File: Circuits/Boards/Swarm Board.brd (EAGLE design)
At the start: 76.2 x 76.2 mm, 95 parts, among them CON1 ISP(2X3), T1 NPN2N2222, T10 TEFT4300, T11 NPN2N2222, T12 NPN2N2222, T13 NPN2N2222, T14 NPN2N2222, T15 NPN2N2222, T16 NPN2N2222, T17 NPN2N2222, T18 NPN2N2222, T2 NPN2N2222, T3 NPN2N2222, T4 TEFT4300, T5 TEFT4300, T6 TEFT4300, T7 TEFT4300, T8 TEFT4300, T9 TEFT4300, U1 ATMEGA324P, U2 MCP73832SOT-23, U3 TB6552FN/FNG

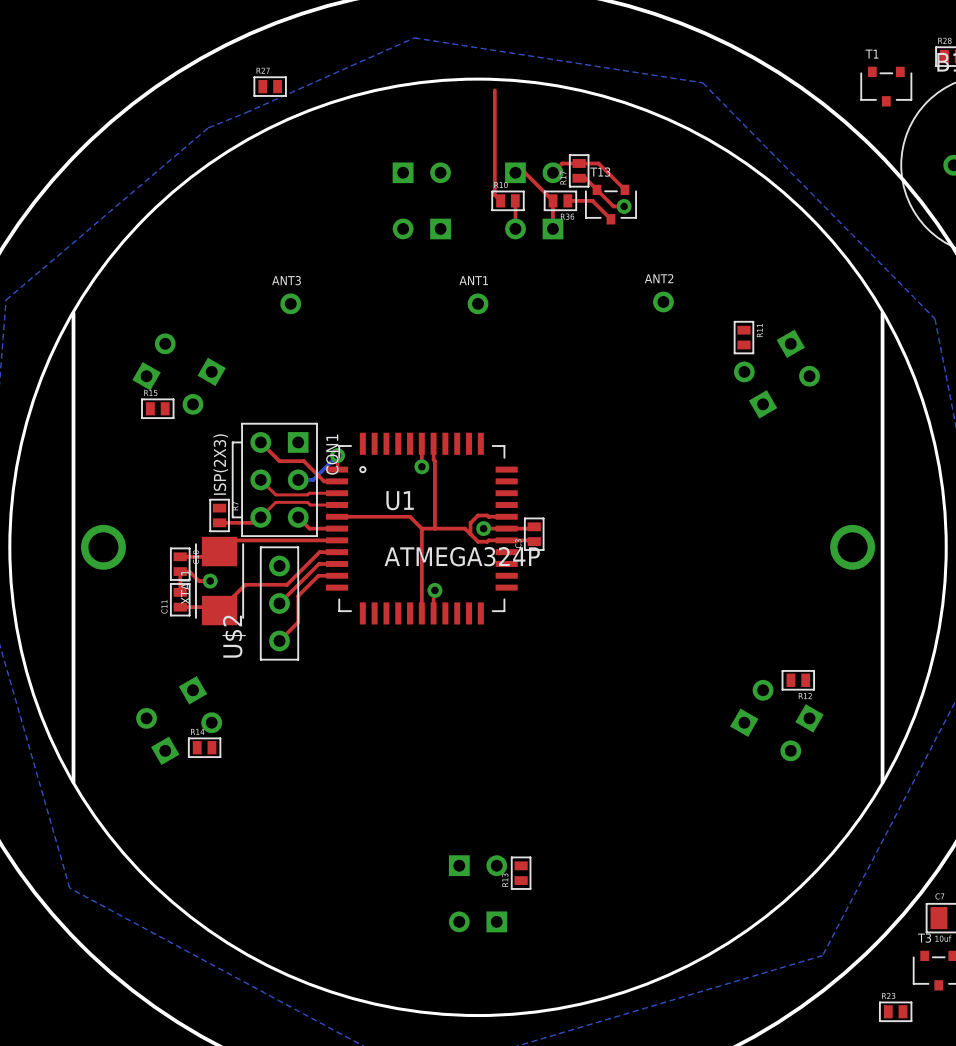
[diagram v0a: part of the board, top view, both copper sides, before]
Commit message: 
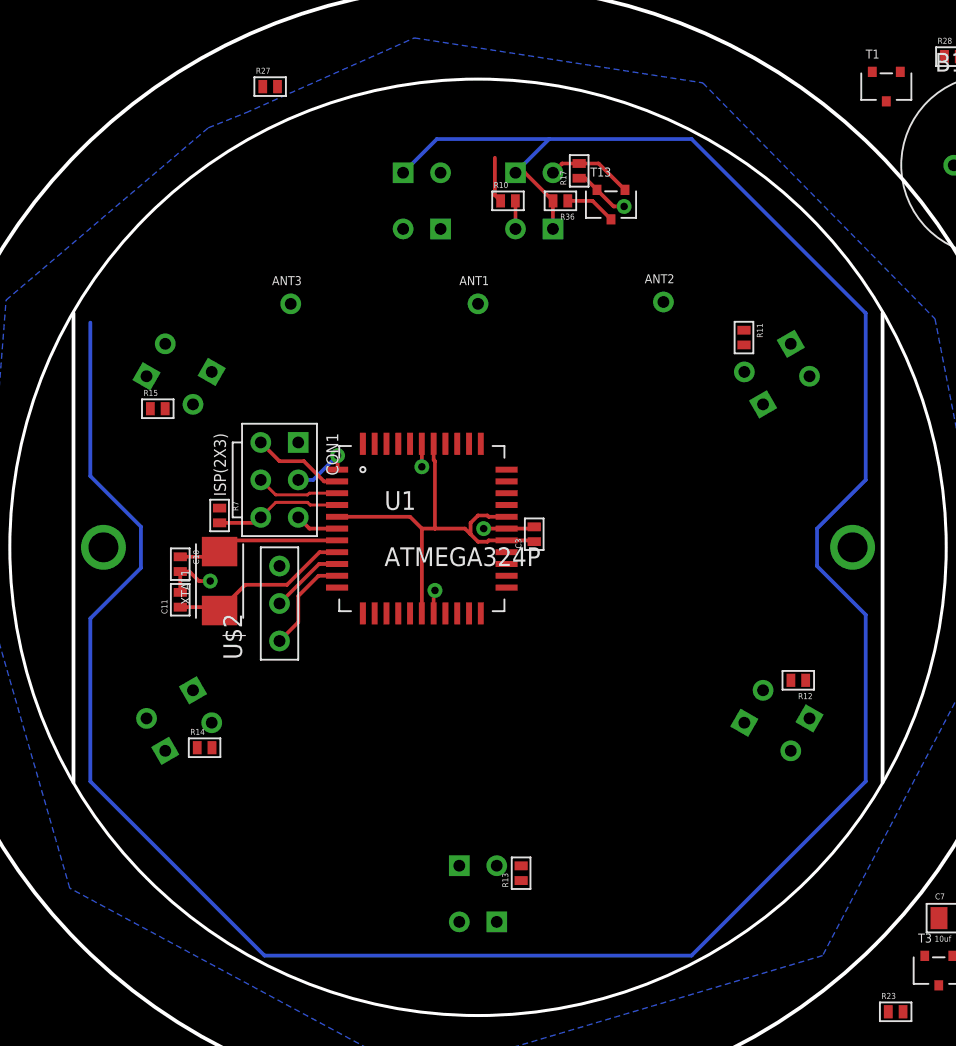
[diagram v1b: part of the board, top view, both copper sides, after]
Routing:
- net +3V: track 34.4 -> 205.6 mm
- net N$10: track 7.66 -> 3.09 mm
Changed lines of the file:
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@@
 <wire x1="36.838" y1="55.245" x2="34.933" y2="57.15" width="0.254" layer="1"/>
 <wire x1="34.933" y1="57.15" x2="34.29" y2="57.15" width="0.254" layer="1"/>
+<wire x1="36.576" y1="59.436" x2="46.228" y2="59.436" width="0.254" layer="16"/>
+<wire x1="46.228" y1="59.436" x2="58.039" y2="47.625" width="0.254" layer="16"/>
+<wire x1="36.576" y1="59.436" x2="34.29" y2="57.15" width="0.254" layer="16"/>
+<wire x1="26.67" y1="57.15" x2="28.956" y2="59.436" width="0.254" layer="16"/>
+<wire x1="28.956" y1="59.436" x2="36.576" y2="59.436" width="0.254" layer="16"/>
+<wire x1="58.039" y1="47.625" x2="58.039" y2="36.322" width="0.254" layer="16"/>
+<wire x1="58.039" y1="36.322" x2="54.737" y2="33.02" width="0.254" layer="16"/>
+<wire x1="54.737" y1="33.02" x2="54.737" y2="30.48" width="0.254" layer="16"/>
+<wire x1="54.737" y1="30.48" x2="58.039" y2="27.178" width="0.254" layer="16"/>
+<wire x1="58.039" y1="27.178" x2="58.039" y2="15.875" width="0.254" layer="16"/>
+<wire x1="58.039" y1="15.875" x2="46.228" y2="4.064" width="0.254" layer="16"/>
+<wire x1="46.228" y1="4.064" x2="17.272" y2="4.064" width="0.254" layer="16"/>
+<wire x1="17.272" y1="4.064" x2="5.461" y2="15.875" width="0.254" layer="16"/>
+<wire x1="5.461" y1="15.875" x2="5.461" y2="26.924" width="0.254" layer="16"/>
+<wire x1="5.461" y1="26.924" x2="8.89" y2="30.353" width="0.254" layer="16"/>
+<wire x1="8.89" y1="30.353" x2="8.89" y2="33.147" width="0.254" layer="16"/>
+<wire x1="8.89" y1="33.147" x2="5.461" y2="36.576" width="0.254" layer="16"/>
+<wire x1="5.461" y1="36.576" x2="5.461" y2="46.99" width="0.254" layer="16"/>
 <wire x1="92.472" y1="42.418" x2="94.168" y2="44.189" width="0" layer="19" extent="1-1"/>
 <wire x1="80.637" y1="46.736" x2="92.472" y2="42.418" width="0" layer="19" extent="1-1"/>
@@
 <wire x1="69.969" y1="64.516" x2="80.7212" y2="56.769" width="0" layer="19" extent="1-1"/>
 <wire x1="64.008" y1="57.658" x2="69.969" y2="64.516" width="0" layer="19" extent="1-1"/>
+<wire x1="58.039" y1="47.625" x2="64.008" y2="57.658" width="0" layer="19" extent="16-16"/>
+<wire x1="29.21" y1="53.34" x2="26.67" y2="57.15" width="0" layer="19" extent="1-1"/>
+<wire x1="9.271" y1="43.350146875" x2="5.461" y2="46.99" width="0" layer="19" extent="16-16"/>
+<wire x1="13.6906" y1="43.64485" x2="9.271" y2="43.350146875" width="0" layer="19" extent="1-1"/>
+<wire x1="52.959" y1="45.54985" x2="58.039" y2="47.625" width="0" layer="19" extent="16-16"/>
+<wire x1="51.0794" y1="41.445146875" x2="52.959" y2="45.54985" width="0" layer="19" extent="1-1"/>
+<wire x1="14.224" y1="34.409" x2="8.89" y2="33.147" width="0" layer="19" extent="1-16"/>
+<wire x1="10.541" y1="17.950146875" x2="5.461" y2="15.875" width="0" layer="19" extent="16-16"/>
+<wire x1="12.4206" y1="22.05485" x2="10.541" y2="17.950146875" width="0" layer="19" extent="1-1"/>
+<wire x1="54.229" y1="20.14985" x2="58.039" y2="15.875" width="0" layer="19" extent="16-16"/>
+<wire x1="49.8094" y1="19.855146875" x2="54.229" y2="20.14985" width="0" layer="19" extent="1-1"/>
+<wire x1="22.19" y1="33.82" x2="14.224" y2="34.409" width="0" layer="19" extent="1-1"/>
+<wire x1="63.008" y1="6.604" x2="58.039" y2="15.875" width="0" layer="19" extent="1-16"/>
+<wire x1="74.565" y1="8.89" x2="63.008" y2="6.604" width="0" layer="19" extent="1-1"/>
+<wire x1="33.02" y1="6.35" x2="46.228" y2="4.064" width="0" layer="19" extent="16-16"/>
+<wire x1="30.48" y1="10.16" x2="33.02" y2="6.35" width="0" layer="19" extent="1-1"/>
 <wire x1="87.003" y1="28.321" x2="92.472" y2="42.418" width="0" layer="19" extent="1-1"/>
 <wire x1="94.226" y1="26.416" x2="87.003" y2="28.321" width="0" layer="19" extent="1-1"/>
@@
 <wire x1="76.846" y1="24.871" x2="77.605" y2="28.321" width="0" layer="19" extent="1-1"/>
 <wire x1="73.795" y1="24.384" x2="76.846" y2="24.871" width="0" layer="19" extent="1-1"/>
-<wire x1="74.565" y1="8.89" x2="73.795" y2="24.384" width="0" layer="19" extent="1-1"/>
-<wire x1="63.008" y1="6.604" x2="74.565" y2="8.89" width="0" layer="19" extent="1-1"/>
-<wire x1="54.229" y1="20.14985" x2="63.008" y2="6.604" width="0" layer="19" extent="1-1"/>
-<wire x1="49.8094" y1="19.855146875" x2="54.229" y2="20.14985" width="0" layer="19" extent="1-1"/>
-<wire x1="52.959" y1="45.54985" x2="64.008" y2="57.658" width="0" layer="19" extent="1-1"/>
-<wire x1="51.0794" y1="41.445146875" x2="52.959" y2="45.54985" width="0" layer="19" extent="1-1"/>
-<wire x1="36.83" y1="53.34" x2="52.959" y2="45.54985" width="0" layer="19" extent="1-1"/>
-<wire x1="29.21" y1="53.34" x2="34.29" y2="57.15" width="0" layer="19" extent="1-1"/>
-<wire x1="26.67" y1="57.15" x2="29.21" y2="53.34" width="0" layer="19" extent="1-1"/>
-<wire x1="28.74" y1="38.77" x2="29.21" y2="53.34" width="0" layer="19" extent="1-1"/>
-<wire x1="14.224" y1="34.409" x2="22.19" y2="33.82" width="0" layer="19" extent="1-1"/>
-<wire x1="13.6906" y1="43.64485" x2="14.224" y2="34.409" width="0" layer="19" extent="1-1"/>
-<wire x1="9.271" y1="43.350146875" x2="13.6906" y2="43.64485" width="0" layer="19" extent="1-1"/>
-<wire x1="12.4206" y1="22.05485" x2="14.224" y2="34.409" width="0" layer="19" extent="1-1"/>
-<wire x1="10.541" y1="17.950146875" x2="12.4206" y2="22.05485" width="0" layer="19" extent="1-1"/>
-<wire x1="30.48" y1="10.16" x2="27.94" y2="27.27" width="0" layer="19" extent="1-1"/>
-<wire x1="33.02" y1="6.35" x2="30.48" y2="10.16" width="0" layer="19" extent="1-1"/>
 <wire x1="95.361" y1="7.89" x2="97.401" y2="26.289" width="0" layer="19" extent="1-1"/>
-<wire x1="-86.114" y1="-10.922" x2="10.541" y2="17.950146875" width="0" layer="19" extent="1-1"/>
+<wire x1="-86.114" y1="-10.922" x2="5.461" y2="15.875" width="0" layer="19" extent="1-16"/>
 <wire x1="-88.908" y1="-10.922" x2="-86.114" y2="-10.922" width="0" layer="19" extent="1-1"/>
 <wire x1="-91.702" y1="-10.922" x2="-88.908" y2="-10.922" width="0" layer="19" extent="1-1"/>
@@
 <contactref element="R15" pad="1"/>
 <contactref element="T2" pad="3"/>
+<wire x1="33.282" y1="55.245" x2="33.274" y2="55.245" width="0.254" layer="1"/>
+<wire x1="33.274" y1="55.245" x2="32.893" y2="55.626" width="0.254" layer="1"/>
+<wire x1="32.893" y1="55.626" x2="32.893" y2="58.166" width="0.254" layer="1"/>
+<wire x1="33.282" y1="55.245" x2="49.784" y2="46.474" width="0" layer="19" extent="1-1"/>
 <wire x1="53.967" y1="22.733" x2="49.784" y2="46.474" width="0" layer="19" extent="1-1"/>
 <wire x1="34.671" y1="9.152" x2="53.967" y2="22.733" width="0" layer="19" extent="1-1"/>
@@
 <wire x1="9.533" y1="41.148" x2="12.708" y2="18.161" width="0" layer="19" extent="1-1"/>
 <wire x1="81.153" y1="3.318" x2="53.967" y2="22.733" width="0" layer="19" extent="1-1"/>
-<wire x1="33.282" y1="55.245" x2="33.274" y2="55.245" width="0.254" layer="1"/>
-<wire x1="33.274" y1="55.245" x2="32.893" y2="55.626" width="0.254" layer="1"/>
-<wire x1="32.893" y1="55.626" x2="32.893" y2="62.738" width="0.254" layer="1"/>
-<wire x1="32.893" y1="62.738" x2="49.784" y2="46.474" width="0" layer="19" extent="1-16"/>
 </signal>
 <signal name="N$11">

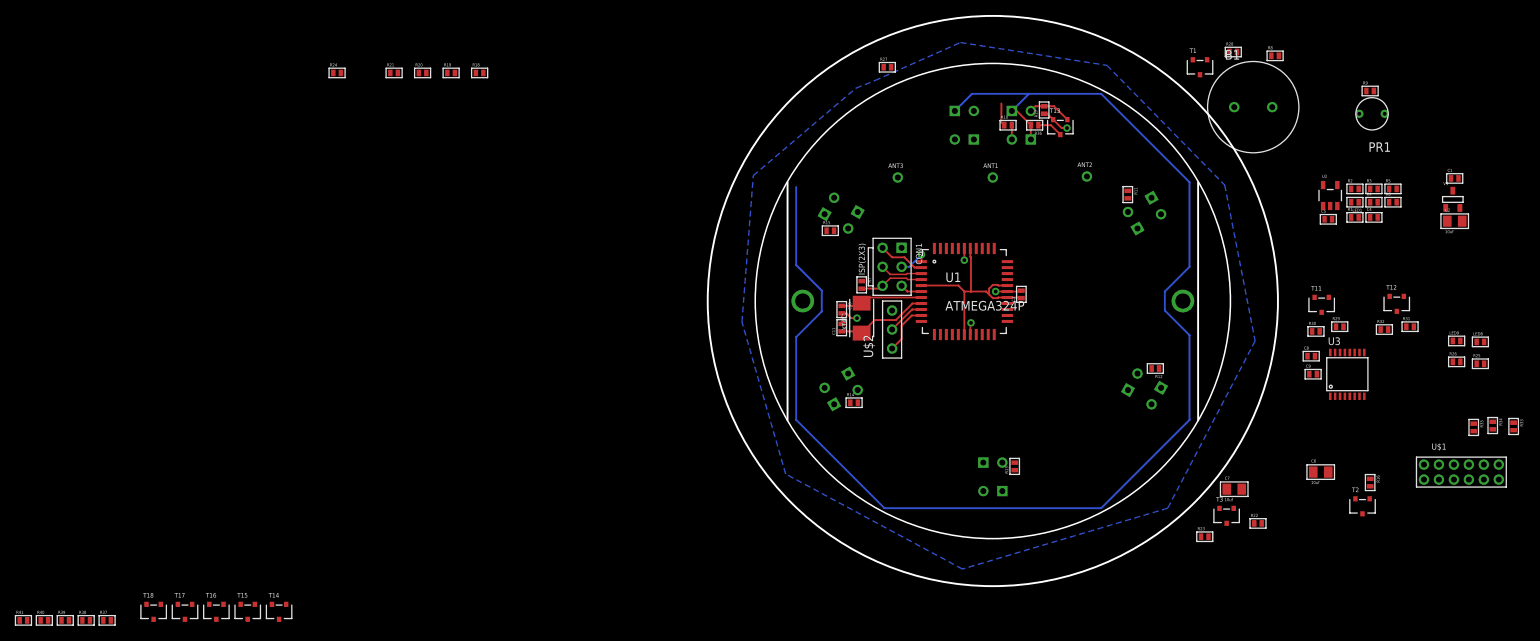
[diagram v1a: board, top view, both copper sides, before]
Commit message: 
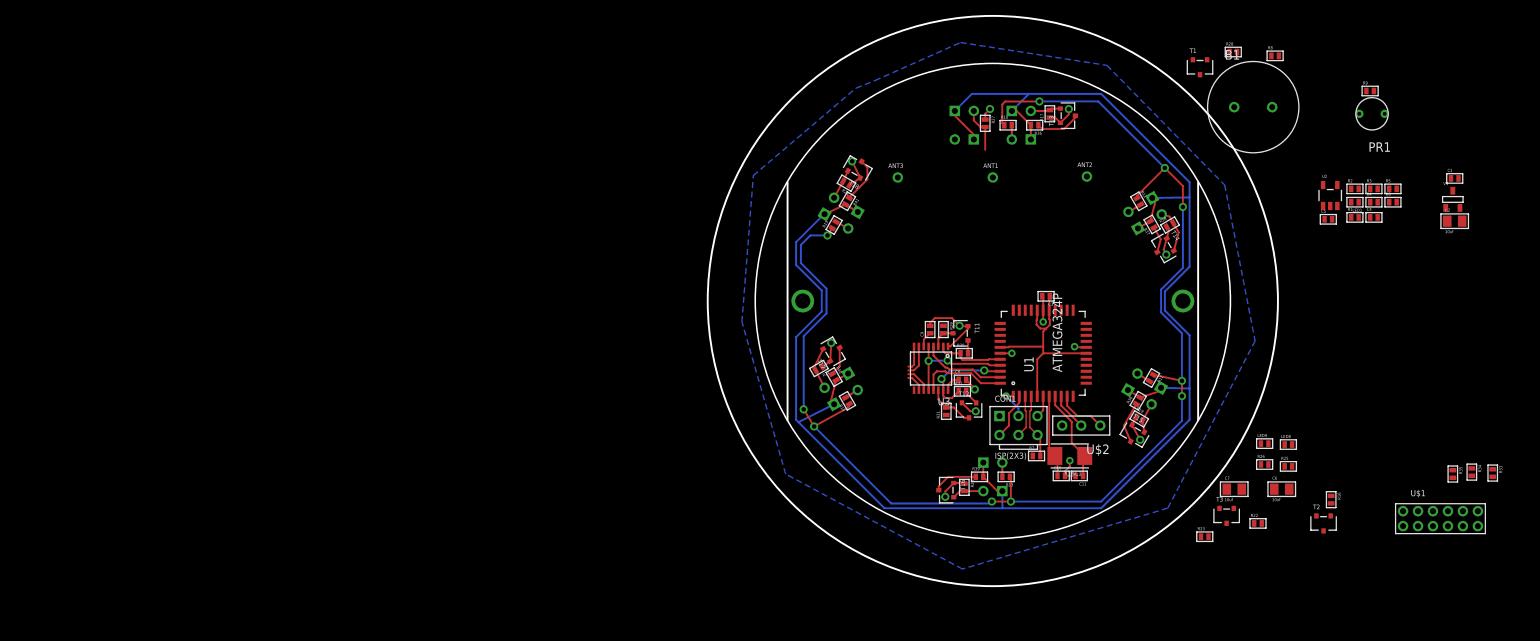
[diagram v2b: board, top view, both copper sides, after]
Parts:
- moved R37 149.3 mm to (53.0, 42.0), turned to 120 degrees
- moved R38 143.6 mm to (51.2, 18.4), turned to 60 degrees
- moved T14 127.8 mm to (54.6, 38.8), turned to 300 degrees
- moved R39 123.7 mm to (30.0, 8.26)
- moved R41 123.5 mm to (12.3, 45.1), turned to 240 degrees
- moved T15 120.8 mm to (50.7, 13.8), turned to 330 degrees
- moved T18 111.2 mm to (13.7, 49.5), turned to 150 degrees
- moved R40 110.4 mm to (10.5, 21.6), turned to 300 degrees
- moved R19 102.9 mm to (51.3, 16.0), turned to 330 degrees
- moved T16 98.9 mm to (25.5, 6.48), turned to 270 degrees
- moved R18 94.5 mm to (55.4, 41.9), turned to 30 degrees
- moved T17 93.3 mm to (10.4, 25.0), turned to 120 degrees
- moved R20 91.1 mm to (27.9, 6.86), turned to 270 degrees
- moved R24 69.6 mm to (12.2, 47.5), turned to 150 degrees
- moved R21 69.2 mm to (8.51, 22.7), turned to 210 degrees
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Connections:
- removed net AIN3: R31.2, T12.3
- net AIN: now also U1.40
- net APWM: now also U1.43
- net BIN: now also U1.42
- net BIN2: now also R31.2, T12.3
- net BPWM: now also U1.44
- net STBY: now also U1.41
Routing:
- net N$10: track 3.09 -> 174.7 mm, vias 0 -> 10
- net +3V: track 205.6 -> 253.3 mm
- net GND: track 17.1 -> 52.4 mm, vias 5 -> 14
- net STBY: track 0.00 -> 15.7 mm, vias 0 -> 2
- net BIN: track 0.00 -> 13.3 mm, vias 0 -> 2
- net BPWM: track 0.00 -> 11.8 mm
- net APWM: track 0.00 -> 11.3 mm
- net AIN: track 0.00 -> 9.15 mm
- net BIN2: track 0.00 -> 6.38 mm
- net DISTANCERECEIVE: track 0.00 -> 6.22 mm
- net N$33: track 0.00 -> 6.18 mm
- net N$38: track 0.00 -> 6.07 mm
- net N$31: track 0.00 -> 5.99 mm
- net N$35: track 0.00 -> 5.81 mm
- net N$30: track 0.00 -> 5.63 mm
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
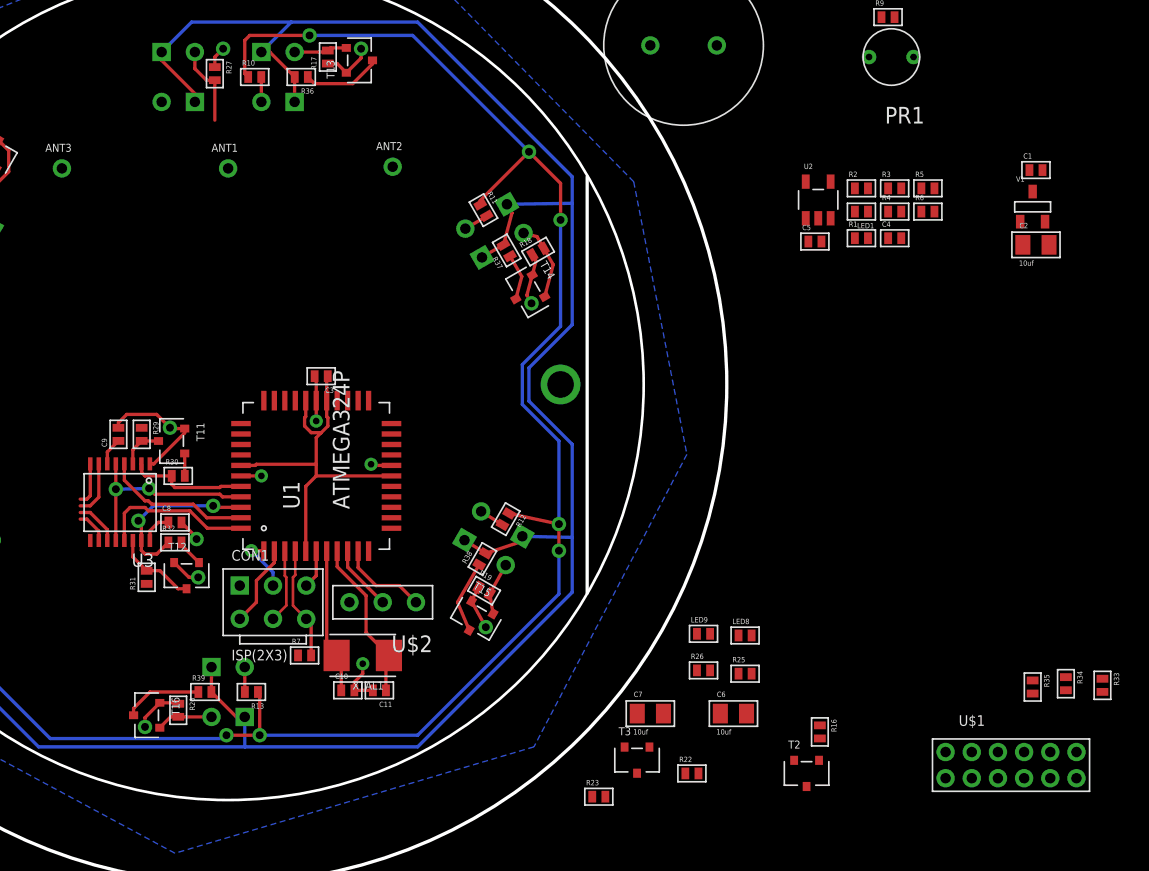
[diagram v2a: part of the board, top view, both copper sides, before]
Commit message: 
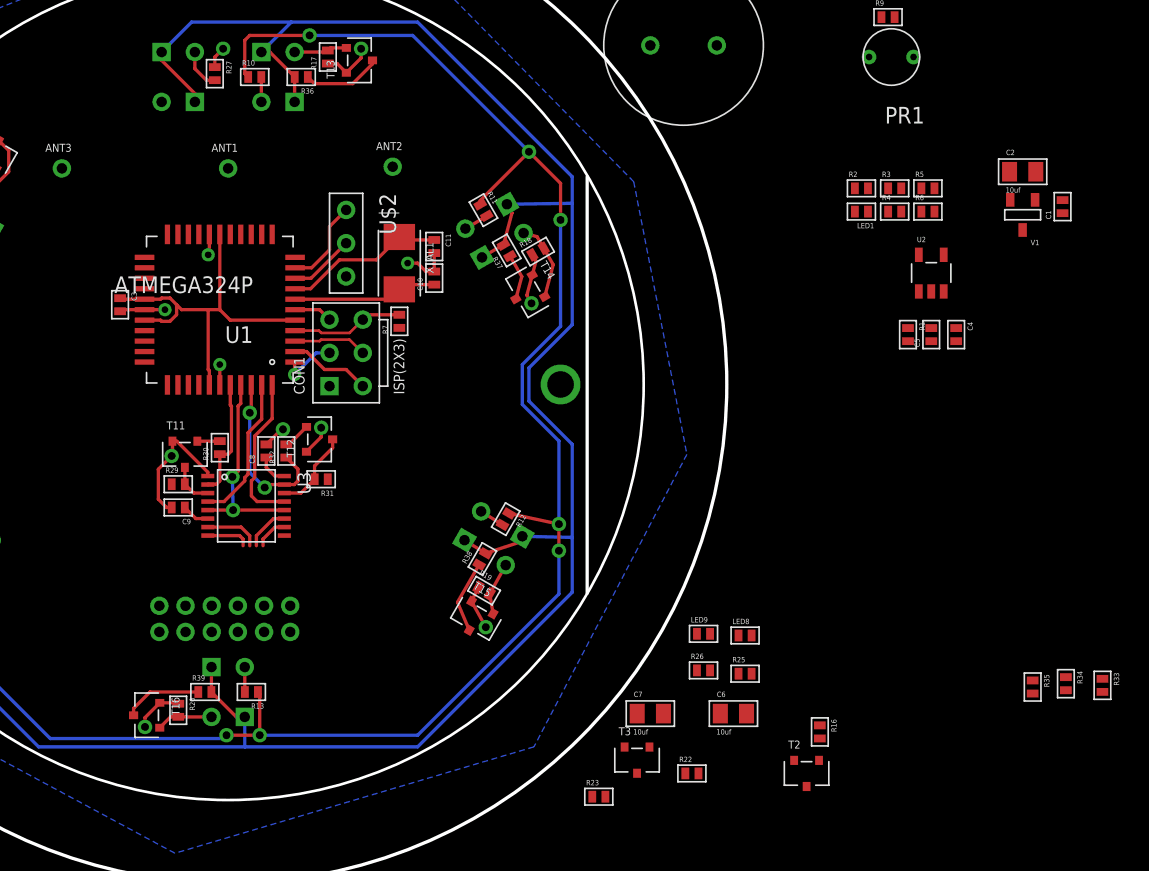
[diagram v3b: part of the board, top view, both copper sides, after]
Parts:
- moved U$1 61.1 mm to (31.5, 13.8), flipped to the bottom
- moved C11 34.2 mm to (47.5, 42.3), turned to 270 degrees
- moved C10 32.2 mm to (47.5, 39.9), turned to 90 degrees
- moved XTAL1 30.1 mm to (44.8, 41.0), turned to 270 degrees
- moved U$2 27.6 mm to (40.8, 42.5), turned to 270 degrees
- moved R7 26.5 mm to (44.8, 36.6), turned to 90 degrees
- moved CON1 19.9 mm to (40.8, 34.2), turned to 90 degrees
- moved C3 16.3 mm to (23.5, 37.8), turned to 270 degrees
- moved R31 15.3 mm to (38.9, 24.5), turned to 180 degrees
- moved U1 14.7 mm to (31.1, 37.5), turned to 180 degrees
- moved T12 14.5 mm to (38.7, 27.6), turned to 90 degrees
- moved C5 11.4 mm to (85.5, 35.6), turned to 90 degrees
- moved R32 11.0 mm to (36.2, 26.7), turned to 90 degrees
- moved U2 10.3 mm to (85.5, 40.3)
- moved U3 9.66 mm to (33.1, 22.5), turned to 270 degrees
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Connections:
- net BUMPER: now also U1.35; no longer U1.33
- net DISTANCELED: now also U1.32
- net DISTANCERECEIVE: now also U1.31; no longer U1.32
- net IRENABLE: now also U1.34
- net LIGHTSENSE: now also U1.33; no longer U1.36
- net LINESENSE1: now also U1.37; no longer U1.35
- net LINESENSE2: now also U1.36; no longer U1.34
- net VSENSE: now also U1.30; no longer U1.37
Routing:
- net DISTANCERECEIVE: track 6.22 -> 3.17 mm
